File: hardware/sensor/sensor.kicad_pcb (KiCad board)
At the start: 2 copper layers, 35 parts, among them IC1 ATTINY202-SSN, IC2 Si4012-C1001GTR, IC3 TPS3839L30DBZR, J1 M20-9770342

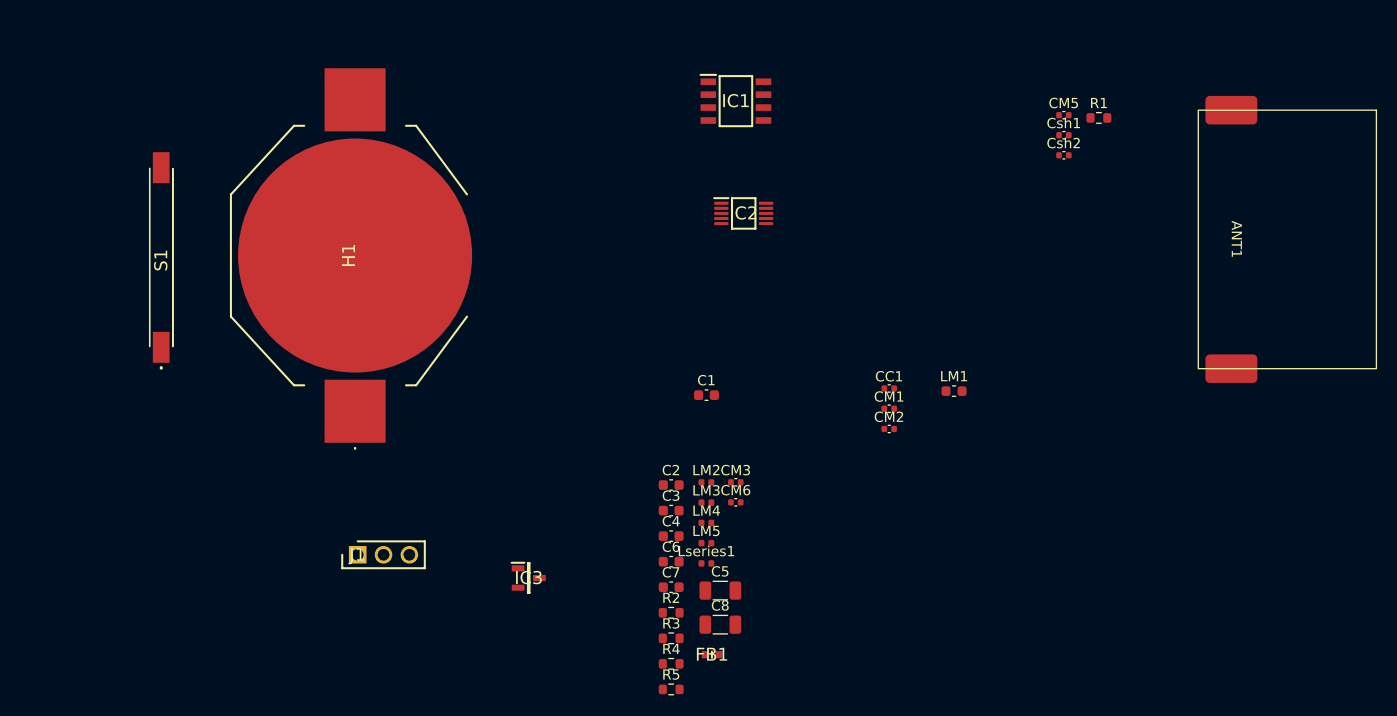
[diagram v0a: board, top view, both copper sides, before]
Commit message: EG-22 Major (bigger) components placed. Missing the balun and antenna pi-matching circuit.
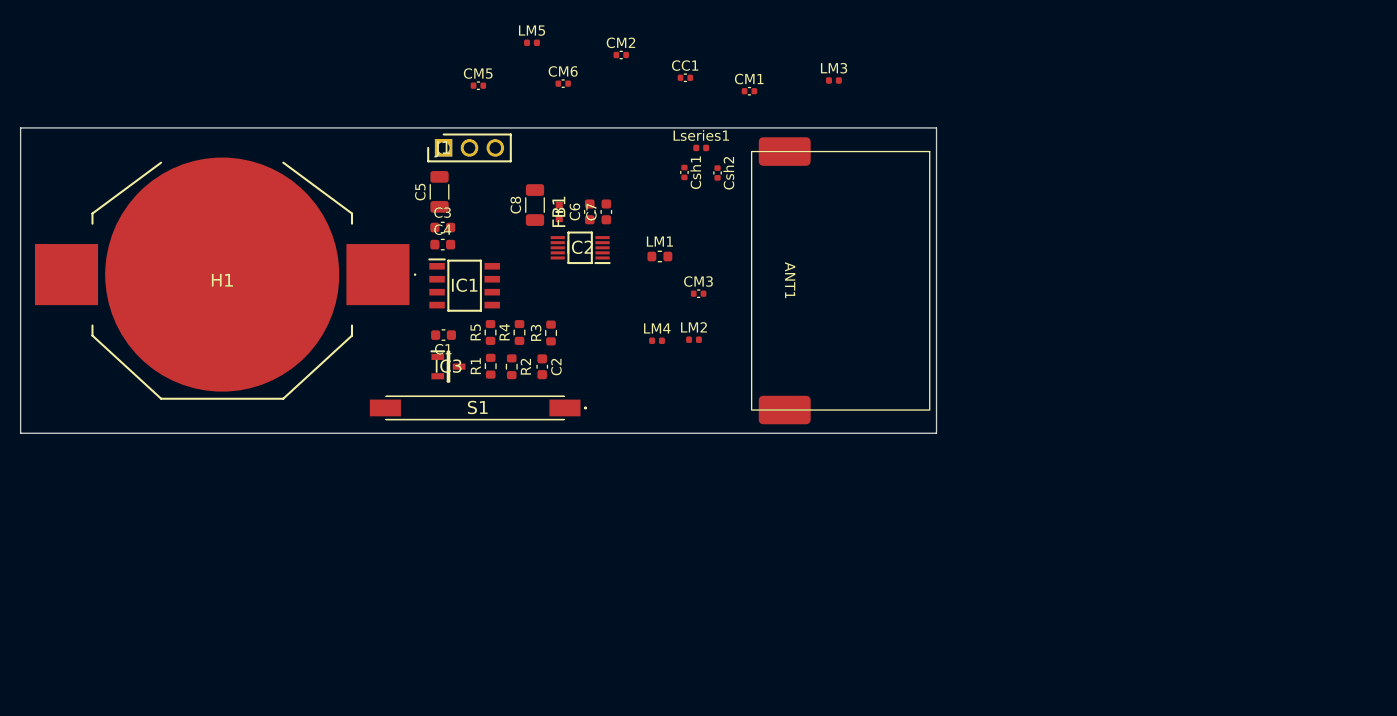
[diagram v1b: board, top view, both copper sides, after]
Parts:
- moved R1 64.6 mm to (64.6, 48.3), turned to 90 degrees
- moved CM5 57.6 mm to (63.4, 20.7)
- moved LM5 52.1 mm to (68.7, 16.5)
- moved C5 47.9 mm to (59.6, 31.1), turned to 90 degrees
- moved FB1 46.0 mm to (71.4, 33.1), turned to -90 degrees
- moved CM2 45.2 mm to (77.5, 17.7)
- moved C8 45.1 mm to (69.0, 32.4), turned to 90 degrees
- moved CM6 44.5 mm to (71.8, 20.5)
- moved ANT1 44.1 mm to (93.5, 39.9)
- moved LM3 43.3 mm to (98.4, 20.2)
- moved J1 40.9 mm to (60.0, 26.8)
- moved Lseries1 40.8 mm to (85.3, 26.8)
- moved R5 39.3 mm to (64.6, 45.0), turned to 90 degrees
- moved Csh1 37.5 mm to (83.7, 29.2), turned to -90 degrees
- moved C7 37.4 mm to (76.0, 33.1), turned to 90 degrees
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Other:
- board outline added: 90 x 30 mm

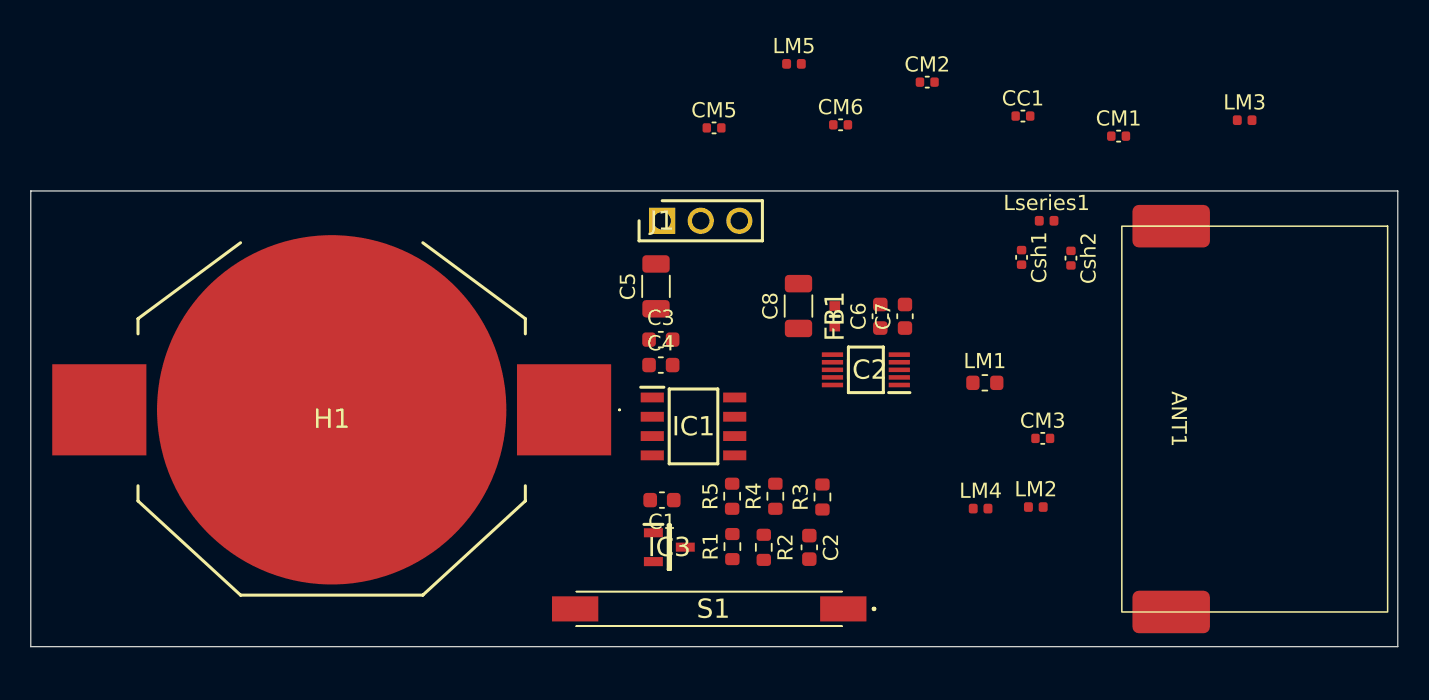
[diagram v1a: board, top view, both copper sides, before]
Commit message: EG-22 All components placed, battery counter yard changed. No connections, and not final places for all components.
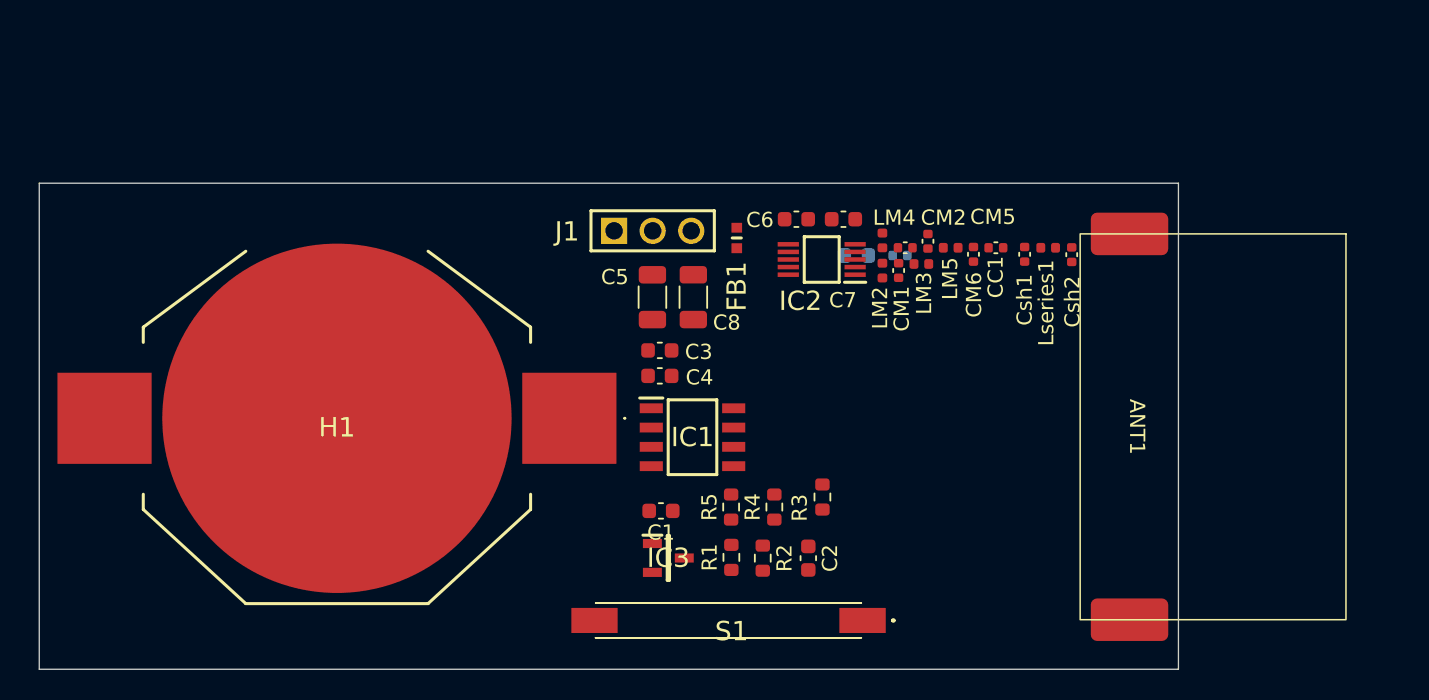
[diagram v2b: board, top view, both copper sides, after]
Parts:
- CM3, LM1: moved to B.Cu
- moved LM3 23.3 mm to (77.1, 29.7)
- moved LM4 18.8 mm to (74.5, 28.1), turned to -90 degrees
- moved LM2 18.6 mm to (74.5, 30.1), turned to -90 degrees
- moved CM1 17.0 mm to (75.6, 30.1), turned to -90 degrees
- moved CM5 15.9 mm to (77.5, 28.2), turned to 90 degrees
- moved LM5 15.9 mm to (79.0, 28.6), turned to 180 degrees
- moved CM3 15.3 mm to (75.7, 29.1)
- moved CM6 12.2 mm to (80.5, 29.0), turned to -90 degrees
- moved LM1 11.9 mm to (72.8, 29.1)
- moved CM2 11.0 mm to (76.0, 28.6), turned to 180 degrees
- moved CC1 8.85 mm to (82.0, 28.6), turned to 180 degrees
- moved C6 8.45 mm to (68.8, 26.7), turned to 180 degrees
- moved FB1 8.26 mm to (64.9, 28.0)
- moved IC2 7.82 mm to (70.5, 29.4)
- moved C7 7.56 mm to (71.9, 26.7), turned to 180 degrees
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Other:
- board size 90 x 30 mm -> 75 x 32 mm

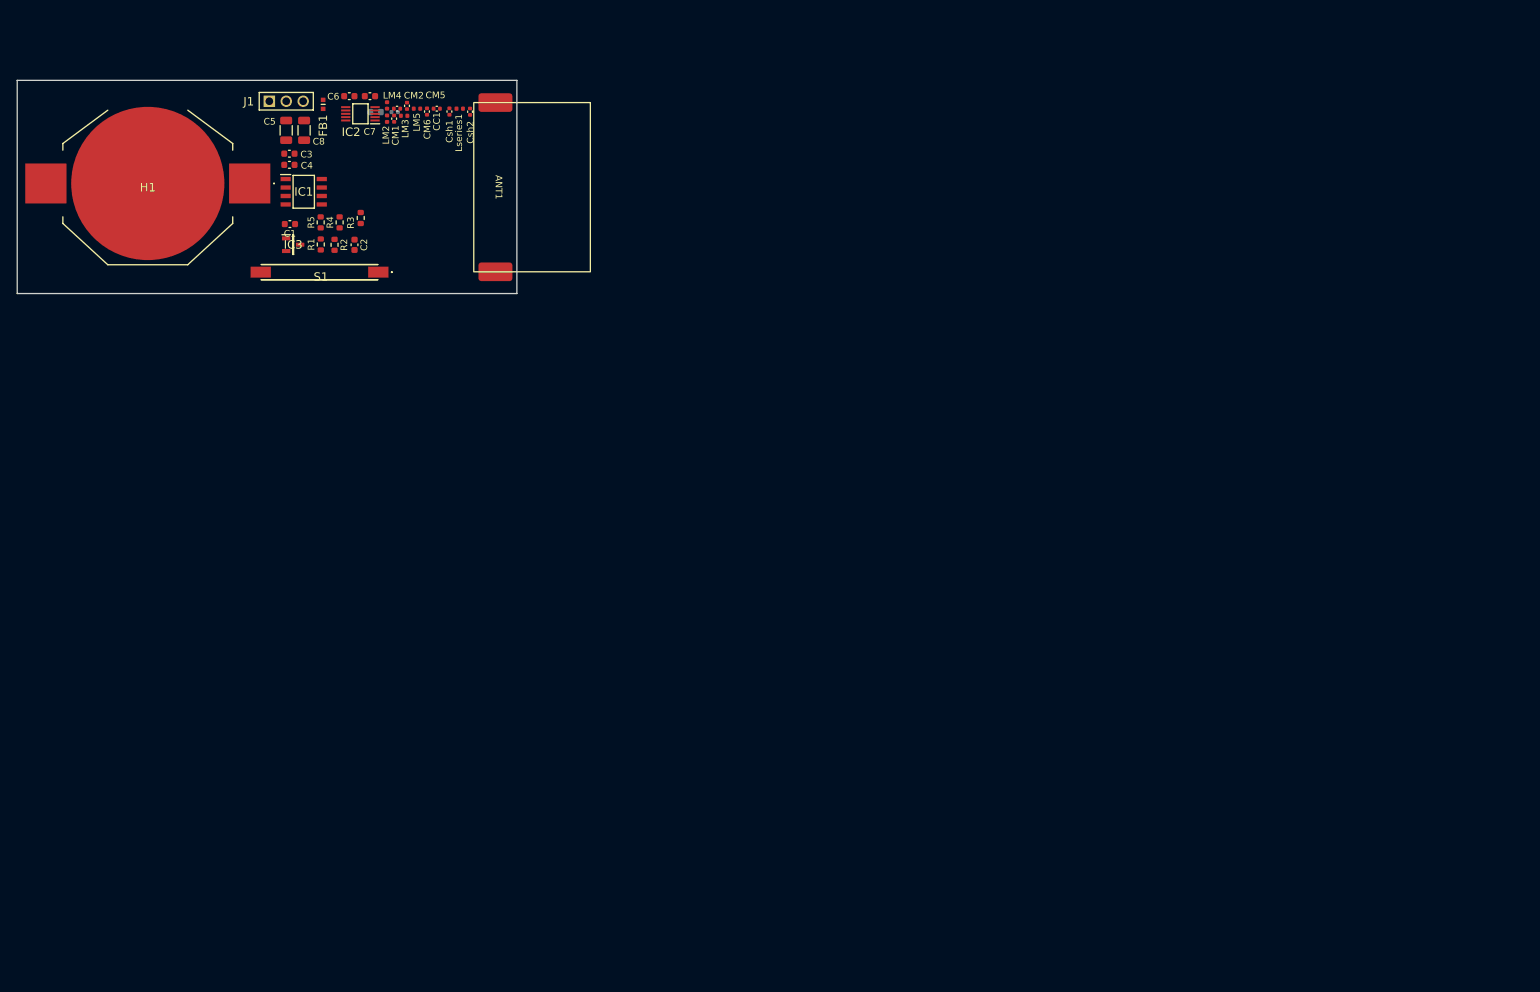
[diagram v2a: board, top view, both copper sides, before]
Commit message: EG-22 All components places frozen. No connections yet.
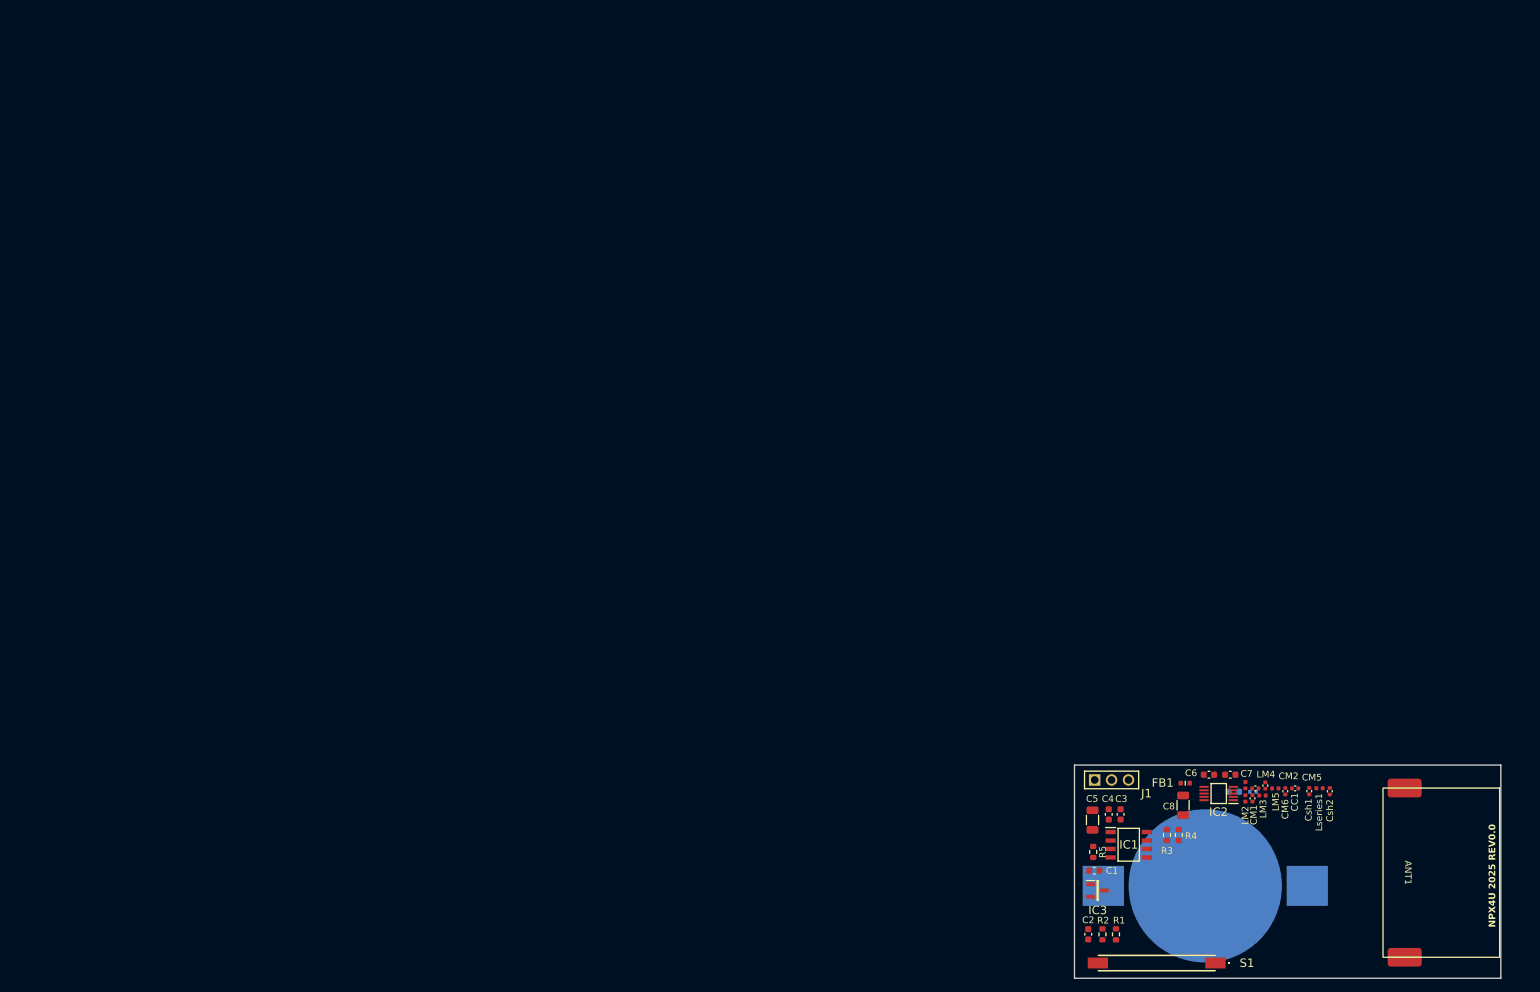
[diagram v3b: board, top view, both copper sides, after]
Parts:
- H1: moved to B.Cu
- moved H1 190.6 mm to (197.3, 145.3)
- moved ANT1 170.9 mm to (227.3, 143.3)
- moved C8 166.4 mm to (194.0, 133.2), turned to -90 degrees
- moved FB1 164.7 mm to (194.3, 129.8), turned to 180 degrees
- moved Csh1 164.5 mm to (212.9, 131.0)
- moved Csh2 164.5 mm to (216.0, 131.1)
- moved Lseries1 164.5 mm to (214.5, 130.6)
- moved C7 164.5 mm to (201.1, 128.6)
- moved C6 164.4 mm to (197.9, 128.6)
- moved CM1 164.3 mm to (204.4, 132.1)
- moved LM1 164.3 mm to (201.6, 131.1)
- moved LM2 164.3 mm to (203.3, 132.1)
- moved LM4 164.3 mm to (203.3, 130.1)
- moved CC1 164.3 mm to (210.8, 130.6)
- moved CM2 164.3 mm to (204.8, 130.6)
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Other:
- board size 75 x 32 mm -> 64 x 32 mm
- board text added: "NPX4U 2025 REV0.0"

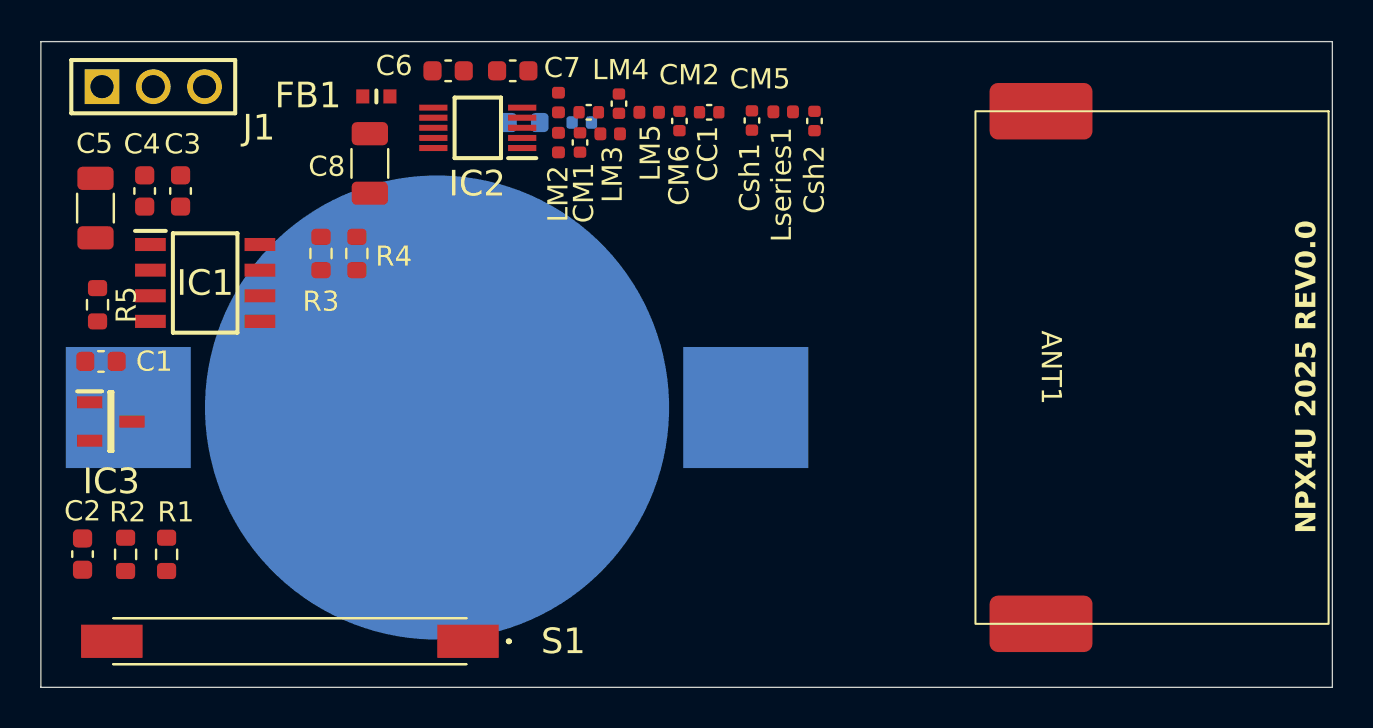
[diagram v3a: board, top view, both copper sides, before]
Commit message: EG-22 All Components connected, except ground and VDD, RF_VDD planes and CPWG to antenna.
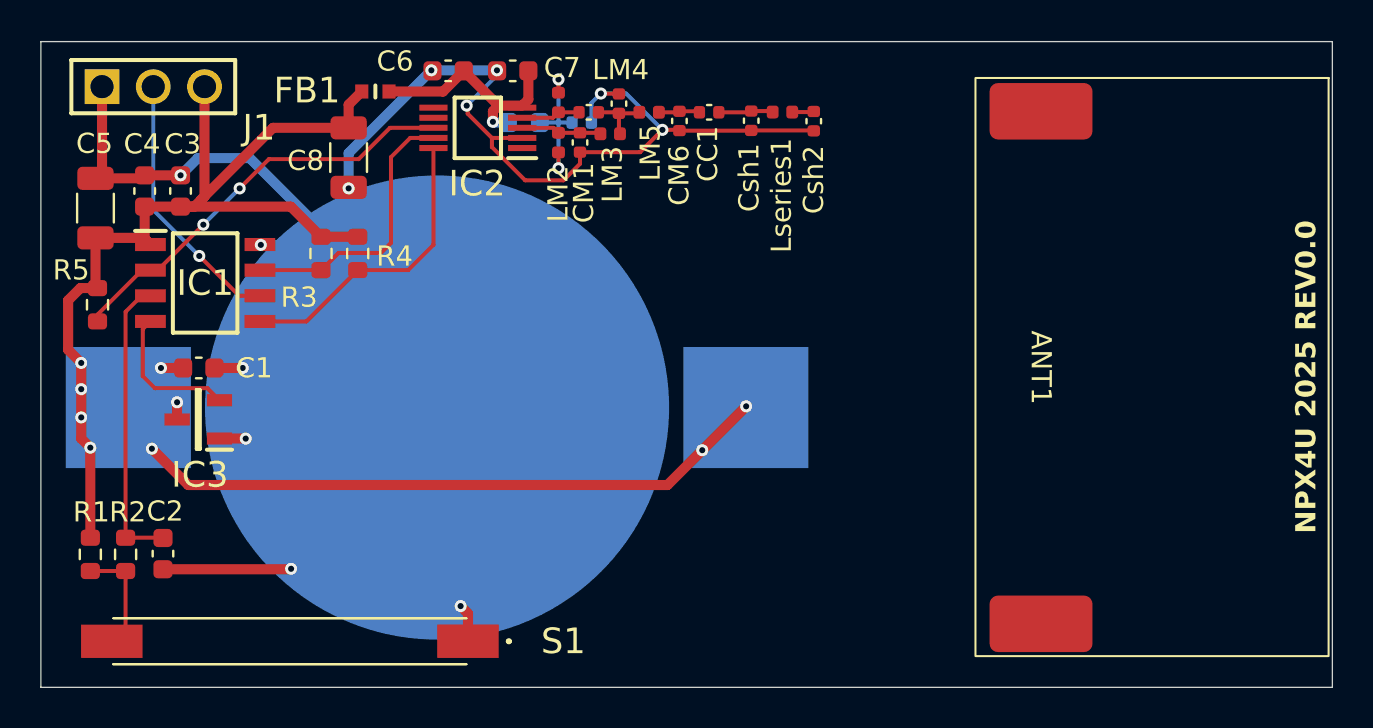
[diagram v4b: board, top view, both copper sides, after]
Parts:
- moved C1 4.86 mm to (185.5, 143.3), turned to 0 degrees
- moved IC3 4.33 mm to (185.5, 145.8), turned to 180 degrees
- moved C2 3.99 mm to (183.8, 152.5)
- moved R1 3.78 mm to (180.2, 152.5)
- moved C8 1.09 mm to (192.9, 132.9)
- moved FB1 0.25 mm to (194.3, 129.6)
- turned Lseries1 to 180 degrees
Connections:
- IC1 pad 2: LOW_BAT -> SDN
- IC1 pad 4: SDN -> LOW_BAT
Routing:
- net GND: track 0.00 -> 115.9 mm, vias 0 -> 12
- net 3.0V: track 0.00 -> 84.1 mm, vias 0 -> 9
- net SDN: track 0.00 -> 21.3 mm, vias 0 -> 2
- net WND: track 0.00 -> 15.1 mm
- net SDA: track 0.00 -> 15.0 mm
- net SCL: track 0.00 -> 14.0 mm
- net UPDI: track 0.00 -> 13.2 mm, vias 0 -> 1
- net RF_VDD: track 0.00 -> 11.2 mm, vias 0 -> 1
- net Net-(CM3-Pad1): track 0.00 -> 7.45 mm, vias 0 -> 2
- net LOW_BAT: track 0.00 -> 7.16 mm
- net Net-(R1-Pad1): track 0.00 -> 5.51 mm
- net TXM: track 0.00 -> 4.00 mm
- net Net-(CM2-Pad1): track 0.00 -> 3.11 mm
- net TXP: track 0.00 -> 2.93 mm
- net Net-(CC1-Pad1): track 0.00 -> 2.71 mm
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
